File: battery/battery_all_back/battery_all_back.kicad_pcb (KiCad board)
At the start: 2 copper layers, 20 parts

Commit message: update battery all back
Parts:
- moved BAT_C2 4.74 mm to (-2.50, 8.00)
- moved BAT_R1 4.74 mm to (-4.00, 8.00)
- moved BAT_R2 4.74 mm to (-1.00, 8.00)
- moved BAT_U1 4.32 mm to (-2.38, 4.00)
- moved BAT_LEDB1 4.05 mm to (5.50, 9.25)
- moved BAT_LEDR1 4.05 mm to (1.00, 9.25)
- moved BAT_R_LEDB1 4.05 mm to (4.00, 9.25)
- moved BAT_R_LEDR1 4.05 mm to (2.50, 9.25)
- moved BAT_TP1 4.01 mm to (3.00, 4.00)
- moved BAT_RA1 3.95 mm to (5.50, -1.25)
- moved BAT_RB1 3.95 mm to (4.00, -1.25)
- moved BAT_R_G1 3.95 mm to (1.00, -1.25)
- moved BAT_R_PRG1 3.95 mm to (2.50, -1.25)
- moved BAT_C3 3.81 mm to (-2.50, 0.00)
- moved BAT_L1 3.81 mm to (-4.00, 0.00)
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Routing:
- net GND: track 96.3 -> 90.0 mm
- net VBAT: track 46.2 -> 50.4 mm
- net VIN: track 20.9 -> 24.7 mm
- net VBUS: track 34.0 -> 37.3 mm
- net VCC: track 12.7 -> 13.9 mm
- net Net-(BAT_U1-LX): track 1.85 -> 2.40 mm

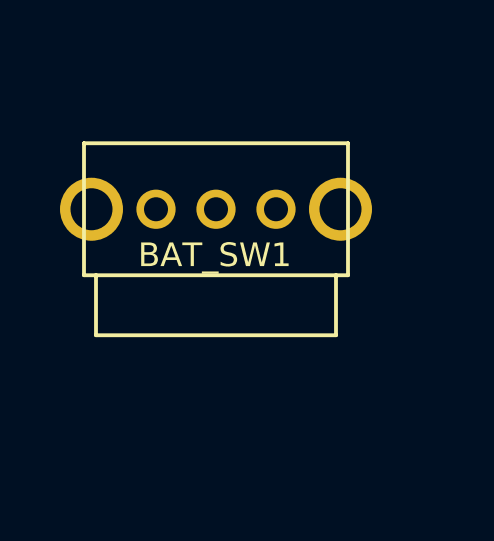
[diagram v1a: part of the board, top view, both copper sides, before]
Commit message: update battery switch symbol
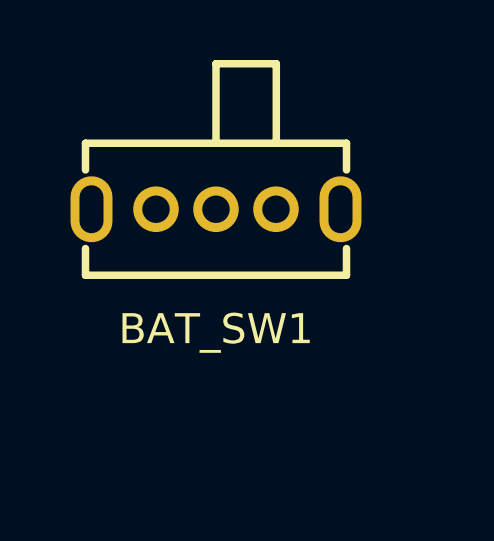
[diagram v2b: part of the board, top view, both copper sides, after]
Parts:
- BAT_C1, BAT_C2, BAT_C3: footprint ErgoCai.pretty:C_0603_1608Metric -> Capacitor_SMD:C_0603_1608Metric
- BAT_L1: footprint ErgoCai.pretty:L_0603_1608Metric -> Inductor_SMD:L_0603_1608Metric
- BAT_Q1: footprint ErgoCai.pretty:SOT-23 -> Package_TO_SOT_SMD:SOT-23
- BAT_SW1: footprint ErgoCai.pretty:SK12D07VG4 -> easyeda2kicad:SW-TH_SK12D07VG4
- BAT_TP1: footprint ErgoCai.pretty:SOIC-8-1EP_3.9x4.9mm_P1.27mm_EP2.29x3mm -> Package_SO:SOIC-8-1EP_3.9x4.9mm_P1.27mm_EP2.29x3mm
- BAT_U1: footprint ErgoCai.pretty:SOT-23-5_L3.0-W1.7-P0.95-LS2.8-BR -> easyeda2kicad:SOT-23-5_L3.0-W1.7-P0.95-LS2.8-BR
- turned BAT_SW1 to 180 degrees
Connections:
- BAT_SW1 pad 2: unconnected-(BAT_SW1-Pad2) -> VBAT

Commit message: remove default battery
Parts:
- BAT_C1, BAT_C2, BAT_C3: footprint Capacitor_SMD:C_0603_1608Metric -> ErgoCai.pretty:C_0603_1608Metric
- BAT_L1: footprint Inductor_SMD:L_0603_1608Metric -> ErgoCai.pretty:L_0603_1608Metric
- BAT_Q1: footprint Package_TO_SOT_SMD:SOT-23 -> ErgoCai.pretty:SOT-23
- BAT_SW1: footprint easyeda2kicad:SW-TH_SK12D07VG4 -> ErgoCai.pretty:SW-TH_SK12D07VG4
- BAT_TP1: footprint Package_SO:SOIC-8-1EP_3.9x4.9mm_P1.27mm_EP2.29x3mm -> ErgoCai.pretty:SOIC-8-1EP_3.9x4.9mm_P1.27mm_EP2.29x3mm
- BAT_U1: footprint easyeda2kicad:SOT-23-5_L3.0-W1.7-P0.95-LS2.8-BR -> ErgoCai.pretty:SOT-23-5_L3.0-W1.7-P0.95-LS2.8-BR
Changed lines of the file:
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@@
 	(net 14 "Net-(BAT_U1-LX)")
 	(net 15 "unconnected-(BAT_SW1-Pad3)")
-	(footprint "easyeda2kicad:SW-TH_SK12D07VG4"
+	(footprint "ErgoCai.pretty:SW-TH_SK12D07VG4"
 		(layer "F.Cu")
 		(at -0.49 -58.65 180)
 		(property "Reference" "BAT_SW1"
-			(at 0 -4 0)
+			(at 0 -4 180)
 			(layer "F.SilkS")
 			(effects
@@
 		)
 		(property "Value" "~"
-			(at 0 4 0)
+			(at 0 4 180)
 			(layer "F.Fab")
 			(effects
@@
 		)
 		(property "Datasheet" "https://lcsc.com/product-detail/Toggle-Switches_SHOU-HAN-SK12D07VG4_C393937.html"
-			(at 0 0 0)
+			(at 0 0 180)
 			(layer "F.Fab")
 			(hide yes)
@@
 		)
 		(property "Description" "Switch, dual pole double throw, separate symbols"
-			(at 0 0 0)
+			(at 0 0 180)
 			(layer "F.Fab")
 			(hide yes)
@@
 		)
 		(fp_text user "${REFERENCE}"
-			(at 0 0 0)
+			(at 0 0 180)
 			(layer "F.Fab")
 			(effects
@@
 		)
 	)
-	(footprint "easyeda2kicad:SOT-23-5_L3.0-W1.7-P0.95-LS2.8-BR"
+	(footprint "ErgoCai.pretty:SOT-23-5_L3.0-W1.7-P0.95-LS2.8-BR"
 		(layer "B.Cu")
 		(at -2.38 4 180)
@@
 			(layer "Cmts.User")
 		)
+		(fp_line
+			(start 2.05 1.7)
+			(end -2.05 1.7)
+			(stroke
+				(width 0.05)
+				(type solid)
+			)
+			(layer "B.CrtYd")
+		)
+		(fp_line
+			(start 2.05 -1.7)
+			(end 2.05 1.7)
+			(stroke
+				(width 0.05)
+				(type solid)
+			)
+			(layer "B.CrtYd")
+		)
+		(fp_line
+			(start -2.05 1.7)
+			(end -2.05 -1.7)
+			(stroke
+				(width 0.05)
+				(type solid)
+			)
+			(layer "B.CrtYd")
+		)
+		(fp_line
+			(start -2.05 -1.7)
+			(end 2.05 -1.7)
+			(stroke
+				(width 0.05)
+				(type solid)
+			)
+			(layer "B.CrtYd")
+		)
 		(fp_circle
 			(center 1.4 -1.45)
@@
 		)
 		(embedded_fonts no)
-		(model "${EASYEDA2KICAD}/easyeda2kicad.3dshapes/SOT-23-5_L2.9-W1.6-H1.1-LS2.8-P0.95.wrl"
+		(model "/Users/jinsongc/Development/ErgoCaiLib/3dmodels/SOT-23-5_L2.9-W1.6-H1.1-LS2.8-P0.95.wrl"
 			(offset
 				(xyz 0 -0 -0)
@@
 		)
 	)
-	(footprint "Inductor_SMD:L_0603_1608Metric"
+	(footprint "ErgoCai.pretty:L_0603_1608Metric"
 		(layer "B.Cu")
 		(at -4 0 90)
@@
 		)
 	)
-	(footprint "Package_TO_SOT_SMD:SOT-23"
+	(footprint "ErgoCai.pretty:SOT-23"
 		(layer "B.Cu")
 		(at 0 -18 90)
-		(descr "SOT, 3 Pin (JEDEC TO-236 Var AB https://www.jedec.org/document_search?search_api_views_fulltext=TO-236), generated with kicad-footprint-generator ipc_gullwing_generator.py")
+		(descr "SOT, 3 Pin (https://www.jedec.org/system/files/docs/to-236h.pdf variant AB), generated with kicad-footprint-generator ipc_gullwing_generator.py")
 		(tags "SOT TO_SOT_SMD")
 		(property "Reference" "BAT_Q1"
@@
 		(property "Datasheet" "http://www.aosmd.com/pdfs/datasheet/AO3401A.pdf"
 			(at 0 0 270)
+			(unlocked yes)
 			(layer "B.Fab")
 			(hide yes)
@@
 		(property "Description" "-4.0A Id, -30V Vds, P-Channel MOSFET, SOT-23"
 			(at 0 0 270)
+			(unlocked yes)
 			(layer "B.Fab")
 			(hide yes)
@@
 		(fp_poly
 			(pts
-				(xy -1.1625 1.51) (xy -1.4025 1.84) (xy -0.9225 1.84)
+				(xy -1.1625 1.51) (xy -1.4025 1.84) (xy -0.9225 1.84) (xy -1.1625 1.51)
 			)
 			(stroke
@@
 		)
 		(fp_line
-			(start 0.9 -1.7)
-			(end -0.9 -1.7)
-			(stroke
-				(width 0.05)
-				(type solid)
-			)
-			(layer "B.CrtYd")
-		)
-		(fp_line
-			(start -0.9 -1.7)
-			(end -0.9 -1.5)
-			(stroke
-				(width 0.05)
-				(type solid)
-			)
-			(layer "B.CrtYd")
-		)
-		(fp_line
-			(start -0.9 -1.5)
-			(end -1.93 -1.5)
+			(start 1.92 -1.7)
+			(end 1.92 1.7)
 			(stroke
 				(width 0.05)
@@
 		)
 		(fp_line
-			(start -1.93 -1.5)
-			(end -1.93 1.5)
+			(start -1.92 -1.7)
+			(end 1.92 -1.7)
 			(stroke
 				(width 0.05)
@@
 		)
 		(fp_line
-			(start 1.93 -0.55)
-			(end 0.9 -0.55)
+			(start 1.92 1.7)
+			(end -1.92 1.7)
 			(stroke
 				(width 0.05)
@@
 		)
 		(fp_line
-			(start 0.9 -0.55)
-			(end 0.9 -1.7)
+			(start -1.92 1.7)
+			(end -1.92 -1.7)
 			(stroke
 				(width 0.05)
@@
 		)
 		(fp_line
-			(start 1.93 0.55)
-			(end 1.93 -0.55)
+			(start 0.65 -1.45)
+			(end -0.65 -1.45)
 			(stroke
-				(width 0.05)
-				(type solid)
-			)
-			(layer "B.CrtYd")
-		)
-		(fp_line
-			(start 0.9 0.55)
-			(end 1.93 0.55)
-			(stroke
-				(width 0.05)
+				(width 0.1)
 				(type solid)
 			)
-			(layer "B.CrtYd")
+			(layer "B.Fab")
 		)
 		(fp_line
-			(start -0.9 1.5)
-			(end -0.9 1.7)
+			(start -0.65 -1.45)
+			(end -0.65 1.125)
 			(stroke
-				(width 0.05)
+				(width 0.1)
 				(type solid)
 			)
-			(layer "B.CrtYd")
+			(layer "B.Fab")
 		)
 		(fp_line
-			(start -1.93 1.5)
-			(end -0.9 1.5)
+			(start -0.65 1.125)
+			(end -0.325 1.45)
 			(stroke
-				(width 0.05)
+				(width 0.1)
 				(type solid)
 			)
-			(layer "B.CrtYd")
+			(layer "B.Fab")
 		)
 		(fp_line
-			(start 0.9 1.7)
-			(end 0.9 0.55)
+			(start 0.65 1.45)
+			(end 0.65 -1.45)
 			(stroke
-				(width 0.05)
+				(width 0.1)
 				(type solid)
 			)
-			(layer "B.CrtYd")
+			(layer "B.Fab")
 		)
 		(fp_line
-			(start -0.9 1.7)
-			(end 0.9 1.7)
-			(stroke
-				(width 0.05)
-				(type solid)
-			)
-			(layer "B.CrtYd")
-		)
-		(fp_poly
-			(pts
-				(xy -0.65 1.125) (xy -0.65 -1.45) (xy 0.65 -1.45) (xy 0.65 1.45) (xy -0.325 1.45)
-			)
+			(start -0.325 1.45)
+			(end 0.65 1.45)
 			(stroke
 				(width 0.1)
 				(type solid)
 			)
-			(fill no)
 			(layer "B.Fab")
 		)
@@
 		)
 		(embedded_fonts no)
-		(model "${KICAD9_3DMODEL_DIR}/Package_TO_SOT_SMD.3dshapes/SOT-23.step"
+		(model "${KICAD8_3DMODEL_DIR}/Package_TO_SOT_SMD.3dshapes/SOT-23.wrl"
 			(offset
 				(xyz 0 0 0)
@@
 		)
 	)
-	(footprint "Capacitor_SMD:C_0603_1608Metric"
+	(footprint "ErgoCai.pretty:C_0603_1608Metric"
 		(layer "B.Cu")
 		(at -2.5 8 90)
@@
 		)
 	)
-	(footprint "Capacitor_SMD:C_0603_1608Metric"
+	(footprint "ErgoCai.pretty:C_0603_1608Metric"
 		(layer "B.Cu")
 		(at -2.5 0 -90)
@@
 		)
 	)
-	(footprint "Package_SO:SOIC-8-1EP_3.9x4.9mm_P1.27mm_EP2.29x3mm"
+	(footprint "ErgoCai.pretty:SOIC-8-1EP_3.9x4.9mm_P1.27mm_EP2.29x3mm"
 		(layer "B.Cu")
 		(at 3 4 -90)
@@
 		(property "Datasheet" ""
 			(at 0 0 90)
+			(unlocked yes)
 			(layer "B.Fab")
 			(hide yes)
@@
 		(property "Description" "TP4056"
 			(at 0 0 90)
+			(unlocked yes)
 			(layer "B.Fab")
 			(hide yes)
@@
 		(fp_poly
 			(pts
-				(xy -2.7 2.465) (xy -2.94 2.795) (xy -2.46 2.795)
+				(xy -2.7 2.465) (xy -2.94 2.795) (xy -2.46 2.795) (xy -2.7 2.465)
 			)
 			(stroke
@@
 		)
 		(fp_line
-			(start -2.2 2.7)
-			(end 2.2 2.7)
-			(stroke
-				(width 0.05)
-				(type solid)
-			)
-			(layer "B.CrtYd")
-		)
-		(fp_line
-			(start 2.2 2.7)
-			(end 2.2 2.46)
-			(stroke
-				(width 0.05)
-				(type solid)
-			)
-			(layer "B.CrtYd")
-		)
-		(fp_line
-			(start -3.7 2.46)
-			(end -2.2 2.46)
+			(start -3.7 2.7)
+			(end -3.7 -2.7)
 			(stroke
 				(width 0.05)
@@
 		)
 		(fp_line
-			(start -2.2 2.46)
-			(end -2.2 2.7)
+			(start 3.7 2.7)
+			(end -3.7 2.7)
 			(stroke
 				(width 0.05)
@@
 		)
 		(fp_line
-			(start 2.2 2.46)
-			(end 3.7 2.46)
+			(start -3.7 -2.7)
+			(end 3.7 -2.7)
 			(stroke
 				(width 0.05)
@@
 		)
 		(fp_line
-			(start 3.7 2.46)
-			(end 3.7 -2.46)
+			(start 3.7 -2.7)
+			(end 3.7 2.7)
 			(stroke
 				(width 0.05)
@@
 		)
 		(fp_line
-			(start -3.7 -2.46)
-			(end -3.7 2.46)
+			(start -0.975 2.45)
+			(end 1.95 2.45)
 			(stroke
-				(width 0.05)
-				(type solid)
-			)
-			(layer "B.CrtYd")
-		)
-		(fp_line
-			(start -2.2 -2.46)
-			(end -3.7 -2.46)
-			(stroke
-				(width 0.05)
+				(width 0.1)
 				(type solid)
 			)
-			(layer "B.CrtYd")
+			(layer "B.Fab")
 		)
 		(fp_line
-			(start 2.2 -2.46)
-			(end 2.2 -2.7)
+			(start 1.95 2.45)
+			(end 1.95 -2.45)
 			(stroke
-				(width 0.05)
+				(width 0.1)
 				(type solid)
 			)
-			(layer "B.CrtYd")
+			(layer "B.Fab")
 		)
 		(fp_line
-			(start 3.7 -2.46)
-			(end 2.2 -2.46)
+			(start -1.95 1.475)
+			(end -0.975 2.45)
 			(stroke
-				(width 0.05)
+				(width 0.1)
 				(type solid)
 			)
-			(layer "B.CrtYd")
+			(layer "B.Fab")
 		)
 		(fp_line
-			(start -2.2 -2.7)
-			(end -2.2 -2.46)
+			(start -1.95 -2.45)
+			(end -1.95 1.475)
 			(stroke
-				(width 0.05)
+				(width 0.1)
 				(type solid)
 			)
-			(layer "B.CrtYd")
+			(layer "B.Fab")
 		)
 		(fp_line
-			(start 2.2 -2.7)
-			(end -2.2 -2.7)
-			(stroke
-				(width 0.05)
-				(type solid)
-			)
-			(layer "B.CrtYd")
-		)
-		(fp_poly
-			(pts
-				(xy -1.95 1.475) (xy -1.95 -2.45) (xy 1.95 -2.45) (xy 1.95 2.45) (xy -0.975 2.45)
-			)
+			(start 1.95 -2.45)
+			(end -1.95 -2.45)
 			(stroke
 				(width 0.1)
 				(type solid)
 			)
-			(fill no)
 			(layer "B.Fab")
 		)
@@
 		)
 		(embedded_fonts no)
-		(model "${KICAD9_3DMODEL_DIR}/Package_SO.3dshapes/SOIC-8-1EP_3.9x4.9mm_P1.27mm_EP2.29x3mm.step"
+		(model "${KICAD8_3DMODEL_DIR}/Package_SO.3dshapes/SOIC-8-1EP_3.9x4.9mm_P1.27mm_EP2.29x3mm.wrl"
 			(offset
 				(xyz 0 0 0)
@@
 		)
 	)
-	(footprint "Capacitor_SMD:C_0603_1608Metric"
+	(footprint "ErgoCai.pretty:C_0603_1608Metric"
 		(layer "B.Cu")
 		(at -1 0 -90)

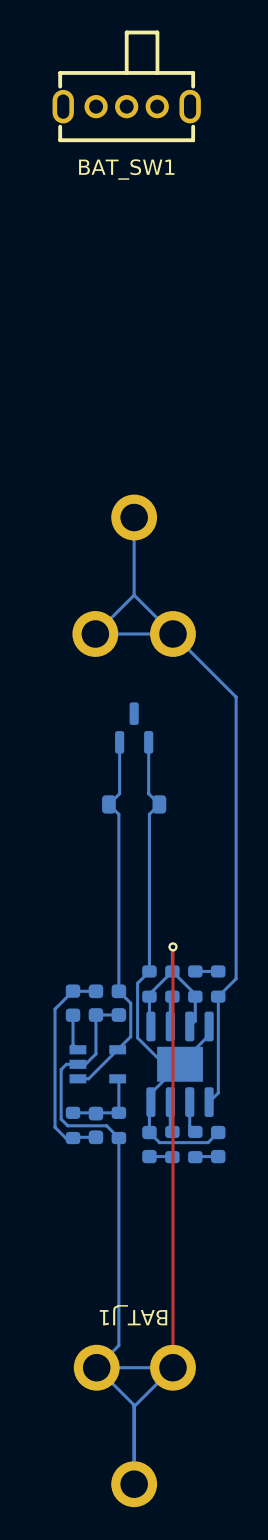
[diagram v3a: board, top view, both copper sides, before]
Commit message: add power switch
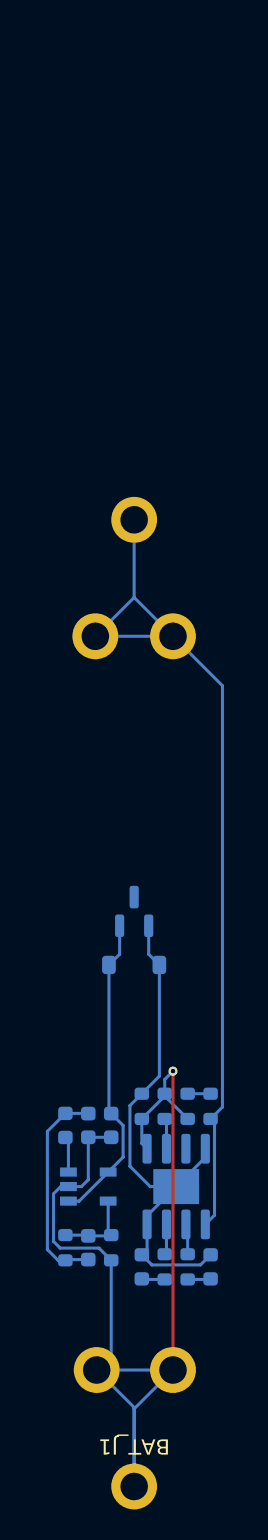
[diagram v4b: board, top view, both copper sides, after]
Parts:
- removed BAT_R_PRG1: 1.2K, ErgoCai.pretty:R_0603_1608Metric
- removed BAT_SW1: ~, ErgoCai.pretty:SW-TH_SK12D07VG4
- added BAT_R_P1: 1.2K, ErgoCai.pretty:R_0603_1608Metric, B.Cu at (2.00, 6.75)
- moved BAT_Q1 12.0 mm to (0.00, -6.00)
- moved BAT_D1 10.5 mm to (0.00, -2.50)
- moved BAT_U1 8.02 mm to (-3.00, 12.0)
- moved BAT_C1 8.02 mm to (-1.50, 8.00)
- moved BAT_C2 8.02 mm to (-3.00, 16.0)
- moved BAT_C3 8.02 mm to (-3.00, 8.00)
- moved BAT_L1 8.02 mm to (-4.50, 8.00)
- moved BAT_LEDB1 8.02 mm to (5.00, 17.2)
- moved BAT_LEDR1 8.02 mm to (0.50, 17.2)
- moved BAT_R1 8.02 mm to (-4.50, 16.0)
- moved BAT_R2 8.02 mm to (-1.50, 16.0)
- moved BAT_RA1 8.02 mm to (5.00, 6.75)
- moved BAT_RB1 8.02 mm to (3.50, 6.75)
- moved BAT_R_G1 8.02 mm to (0.50, 6.75)
- moved BAT_R_LEDB1 8.02 mm to (3.50, 17.2)
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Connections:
- BAT_Q1 pad 3: Net-(BAT_Q1-D) -> VSYS
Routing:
- net GND: track 90.0 -> 71.9 mm
- net VBAT: track 50.4 -> 57.8 mm
- net VIN: track 24.7 -> 20.6 mm
- net VBUS: track 37.3 -> 34.1 mm

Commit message: update to 3.3V tag
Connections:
- net VCC renamed 3.3V
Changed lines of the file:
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@@
 	(net 1 "VBAT")
 	(net 2 "GND")
-	(net 3 "VCC")
+	(net 3 "3.3V")
 	(net 4 "VBUS")
 	(net 5 "ADC_BT")
@@
 			(layers "B.Cu" "B.Mask" "B.Paste")
 			(roundrect_rratio 0.25)
-			(net 3 "VCC")
+			(net 3 "3.3V")
 			(pinfunction "2")
 			(pintype "passive")
@@
 			(layers "B.Cu" "B.Mask" "B.Paste")
 			(roundrect_rratio 0.25)
-			(net 3 "VCC")
+			(net 3 "3.3V")
 			(pintype "passive")
 		)
@@
 			(layers "B.Cu" "B.Mask" "B.Paste")
 			(roundrect_rratio 0.25)
-			(net 3 "VCC")
+			(net 3 "3.3V")
 			(pintype "passive")
 		)
@@
 			(layers "B.Cu" "B.Mask" "B.Paste")
 			(roundrect_rratio 0.25)
-			(net 3 "VCC")
+			(net 3 "3.3V")
 			(pintype "passive")
 		)
